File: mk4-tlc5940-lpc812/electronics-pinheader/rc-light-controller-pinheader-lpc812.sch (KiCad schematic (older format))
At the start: 14 parts, among them J1 Pinheader right-angle 2x17, J2 Pinheader straight 1x06, J3 Pinheader straight 1x06, T9 PMV30UN, U1 LPC812M101JDH20, U2 TLC5940PWP, U3 MCP1703A-3302_SOT23

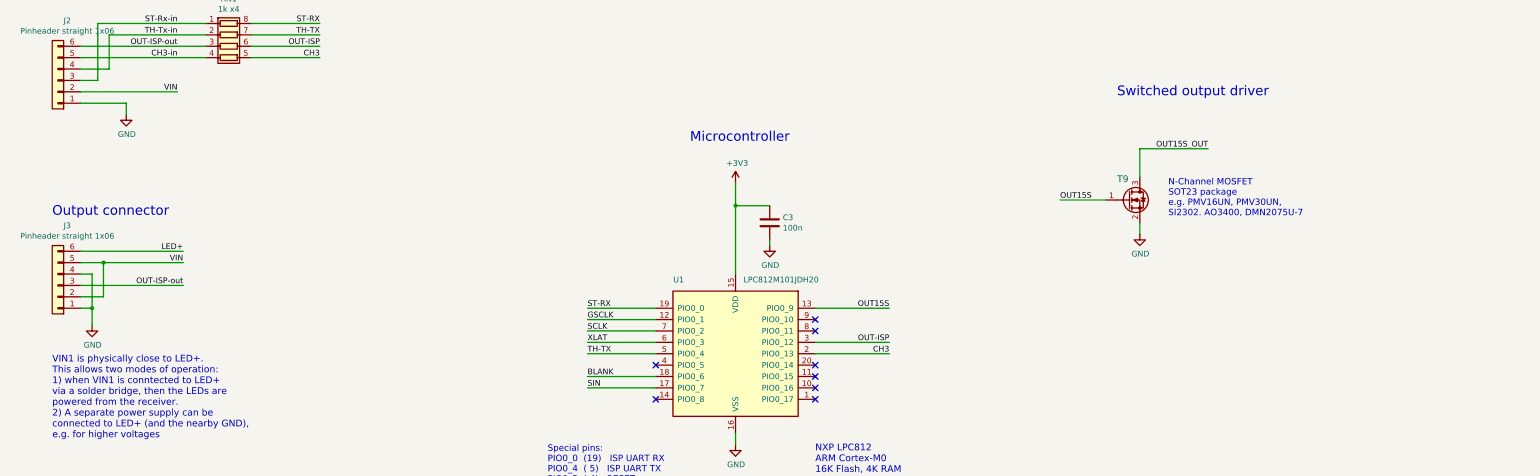
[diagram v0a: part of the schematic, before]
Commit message: Swap VIN and LED+, add version detection
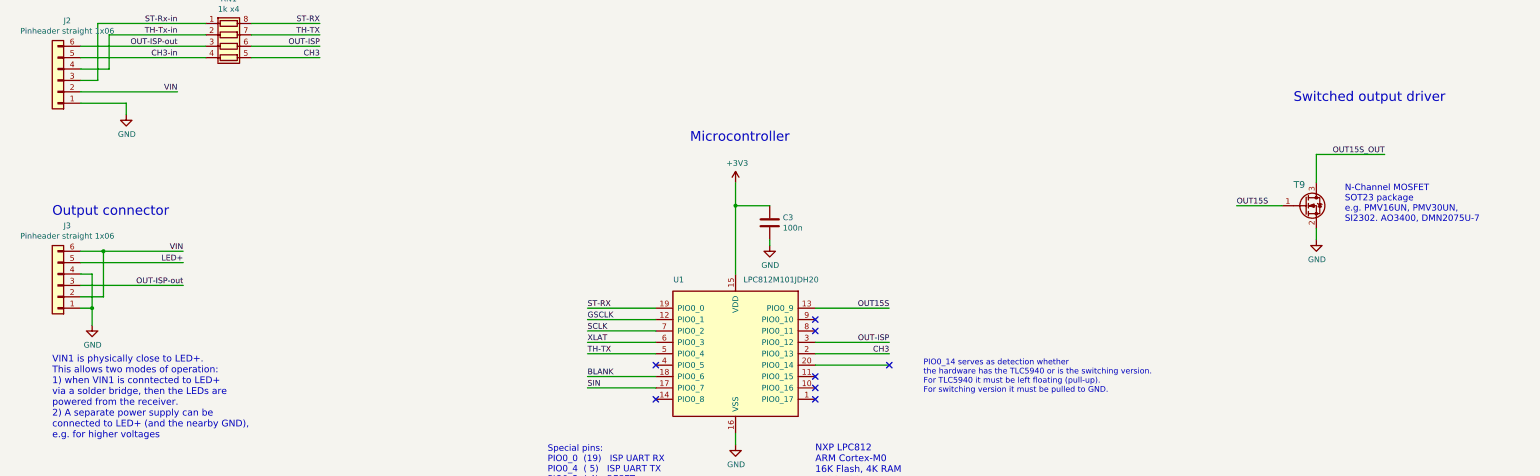
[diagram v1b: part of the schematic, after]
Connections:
- net LED+: now also J3.5 (Pin_5); no longer J3.6 (Pin_6)
- net VIN: now also J3.6 (Pin_6); no longer J3.5 (Pin_5)
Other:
- note added: "PIO0_14 serves as detection whether \nthe hardware has the TLC5940 or is the switching version. \nFor TLC5940 it must be left floating (pull-up).\nFor switching version it must be pulled to GND."
- moved on the sheet: T9
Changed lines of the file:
@@
 GSCLK
 NoConn ~ 7000 8250
+Text Label 2850 7250 2    50   ~ 0
+VIN
 Text Label 2850 7350 2    50   ~ 0
-VIN
-Text Label 2850 7250 2    50   ~ 0
 LED+
 Text Notes 1700 8900 0    59   ~ 0
@@
 $EndComp
 Wire Wire Line
-	1950 7350 2150 7350
-Wire Wire Line
 	1950 7650 2150 7650
-Wire Wire Line
-	2150 7650 2150 7350
-Connection ~ 2150 7350
-Wire Wire Line
-	2150 7350 2850 7350
 Wire Wire Line
 	1950 7450 2050 7450
@@
 Connection ~ 2050 7750
 Wire Wire Line
-	1950 7250 2850 7250
+	1950 7250 2150 7250
 Wire Wire Line
 	14450 2850 14200 2850
@@
 Wire Wire Line
 	6400 8050 7000 8050
-NoConn ~ 8400 8250
 $Comp
 L Device:C C3
@@
 L power:GND #PWR01
 U 1 1 5EEF5842
-P 11250 7100
-F 0 "#PWR01" H 11250 6850 50  0001 C CNN
-F 1 "GND" H 11255 6927 50  0000 C CNN
-F 2 "" H 11250 7100 50  0001 C CNN
-F 3 "" H 11250 7100 50  0001 C CNN
-	1    11250 7100
-	1    0    0    -1
-$EndComp
-Text Notes 11500 6950 0    56   ~ 0
+P 12800 7150
+F 0 "#PWR01" H 12800 6900 50  0001 C CNN
+F 1 "GND" H 12805 6977 50  0000 C CNN
+F 2 "" H 12800 7150 50  0001 C CNN
+F 3 "" H 12800 7150 50  0001 C CNN
+	1    12800 7150
+	1    0    0    -1
+$EndComp
+Text Notes 13050 7000 0    56   ~ 0
 N-Channel MOSFET\nSOT23 package\ne.g. PMV16UN, PMV30UN, \nSI2302. AO3400, DMN2075U-7
-Text Label 10550 6800 0    50   ~ 0
+Text Label 12100 6850 0    50   ~ 0
 OUT15S
 Wire Wire Line
-	10550 6800 10950 6800
-Wire Wire Line
-	11250 7000 11250 7100
+	12100 6850 12500 6850
+Wire Wire Line
+	12800 7050 12800 7150
 $Comp
 L Device:Q_NMOS_GSD T9
 U 1 1 5EEE69E5
-P 11150 6800
-F 0 "T9" H 11050 6950 59  0000 L BNN
-F 1 "PMV30UN" H 11250 6800 59  0001 L BNN
-F 2 "Package_TO_SOT_SMD:SOT-23" H 11150 6800 50  0001 C CNN
-F 3 "https://assets.nexperia.com/documents/data-sheet/PMV30UN.pdf" H 11150 6800 50  0001 C CNN
-	1    11150 6800
+P 12700 6850
+F 0 "T9" H 12600 7000 59  0000 L BNN
+F 1 "PMV30UN" H 12800 6850 59  0001 L BNN
+F 2 "Package_TO_SOT_SMD:SOT-23" H 12700 6850 50  0001 C CNN
+F 3 "https://assets.nexperia.com/documents/data-sheet/PMV30UN.pdf" H 12700 6850 50  0001 C CNN
+	1    12700 6850
 	1    0    0    -1
 $EndComp
@@
 Wire Wire Line
 	1950 5450 3050 5450
-Text Label 11850 6350 2    50   ~ 0
+Text Label 13400 6400 2    50   ~ 0
 OUT15S_OUT
 Text Label 13000 4150 0    50   ~ 0
 OUT15S_OUT
 Wire Wire Line
-	11250 6600 11250 6350
-Wire Wire Line
-	11250 6350 11850 6350
+	12800 6650 12800 6400
+Wire Wire Line
+	12800 6400 13400 6400
 Text Notes 9100 1750 0    85   ~ 0
 LED driver
 Wire Wire Line
 	13000 4150 13700 4150
-Text Notes 11050 5900 0    85   ~ 0
+Text Notes 12600 5950 0    85   ~ 0
 Switched output driver
 $Comp
@@
 	1    0    0    -1
 $EndComp
+Wire Wire Line
+	1950 7350 2850 7350
+Wire Wire Line
+	2150 7650 2150 7250
+Connection ~ 2150 7250
+Wire Wire Line
+	2150 7250 2850 7250
+Wire Wire Line
+	8400 8250 9050 8250
+NoConn ~ 9050 8250
+Text Notes 9350 8500 0    50   ~ 0
+PIO0_14 serves as detection whether \nthe hardware has the TLC5940 or is the switching version. \nFor TLC5940 it must be left floating (pull-up).\nFor switching version it must be pulled to GND.
 $EndSCHEMATC

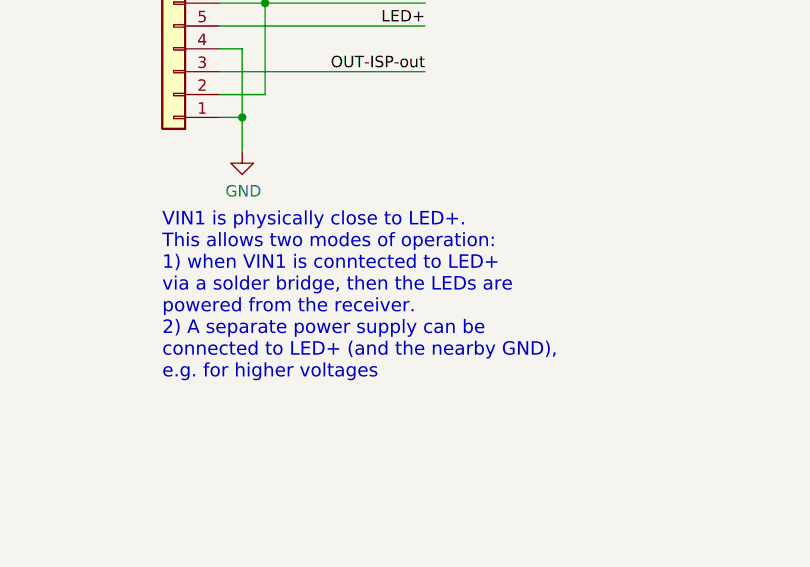
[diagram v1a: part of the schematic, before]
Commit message: Update text regarding jumper use
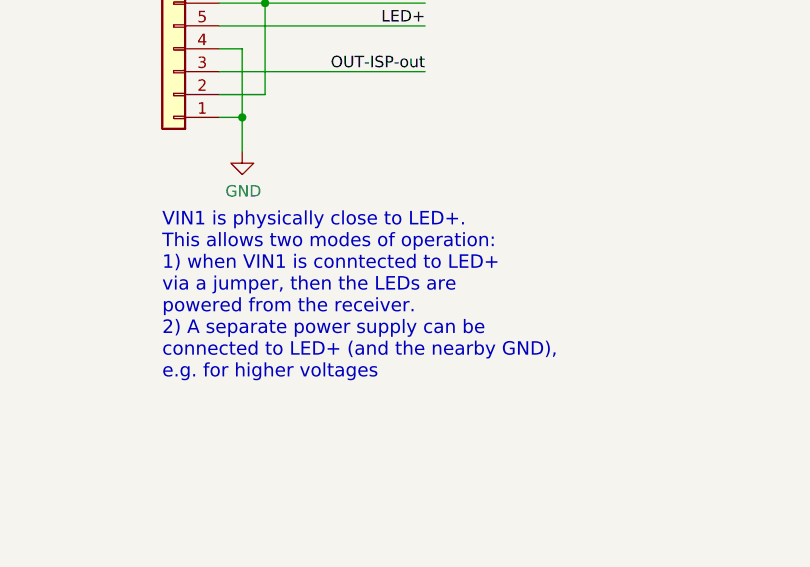
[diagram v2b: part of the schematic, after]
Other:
- note added: "VIN1 is physically close to LED+.\nThis allows two modes of operation:\n1) when VIN1 is conntected to LED+\nvia a jumper, then the LEDs are \npowered from the receiver.\n2) A separate power supply can be \nconnected to LED+ (and the nearby GND),\ne.g. for higher voltages"
- note removed: "VIN1 is physically close to LED+.\nThis allows two modes of operation:\n1) when VIN1 is conntected to LED+\nvia a solder bridge, then the LEDs are \npowered from the receiver.\n2) A separate power supply can be \nconnected to LED+ (and the nearby GND),\ne.g. for higher voltages"
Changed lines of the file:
@@
 LED+
 Text Notes 1700 8900 0    59   ~ 0
-VIN1 is physically close to LED+.\nThis allows two modes of operation:\n1) when VIN1 is conntected to LED+\nvia a solder bridge, then the LEDs are \npowered from the receiver.\n2) A separate power supply can be \nconnected to LED+ (and the nearby GND),\ne.g. for higher voltages
+VIN1 is physically close to LED+.\nThis allows two modes of operation:\n1) when VIN1 is conntected to LED+\nvia a jumper, then the LEDs are \npowered from the receiver.\n2) A separate power supply can be \nconnected to LED+ (and the nearby GND),\ne.g. for higher voltages
 Text Notes 1700 6950 0    85   ~ 0
 Output connector
